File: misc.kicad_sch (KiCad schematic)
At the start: 93 parts, among them CN2 Expansion, CN3 Cartridge, CN5 1P, CN504 AV Out, CN6 1P, IC401 74ACT241, IC701 PIC16F630/18324, IC901 TL974, J1 Barrel_Jack, J2 EXT, Q1 MMBT3904, U1 TPS564257DRLR

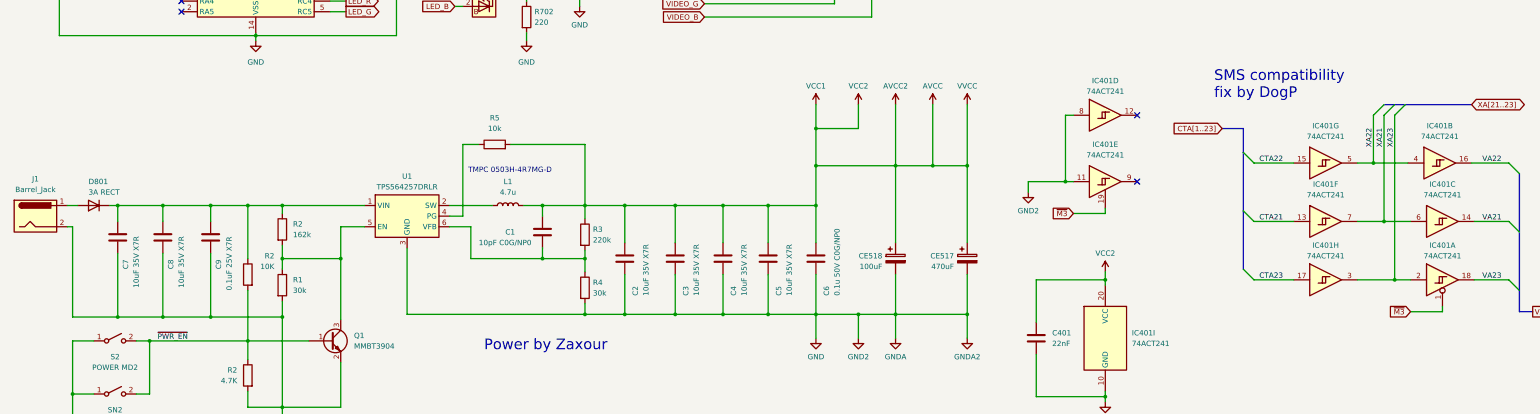
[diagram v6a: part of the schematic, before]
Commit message: More tweaks, documentation. Add hex file for switchless mod.
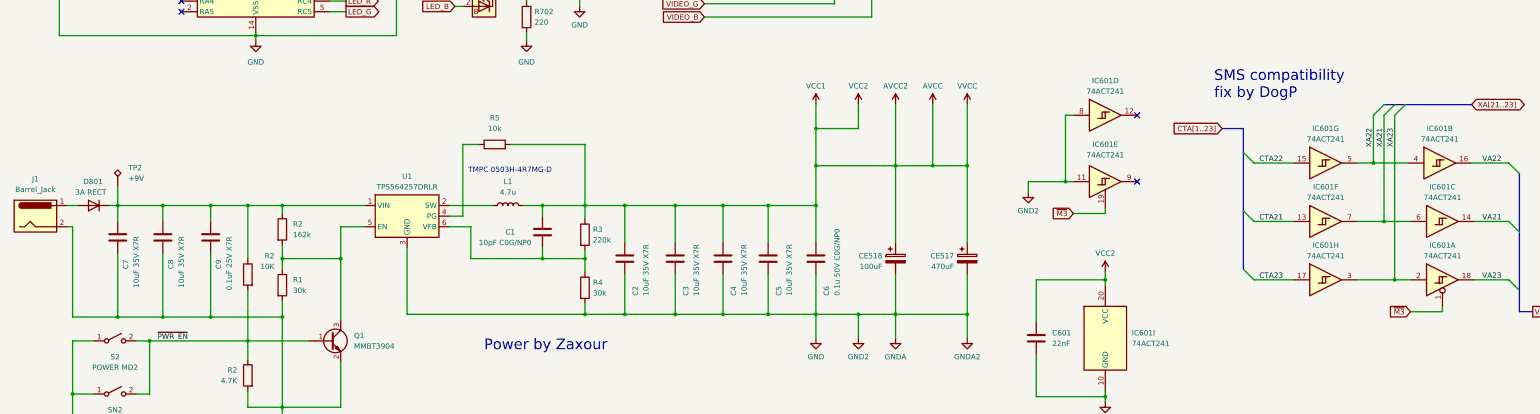
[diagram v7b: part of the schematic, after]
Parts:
- added TP2: +9V, Connector_PinHeader_2.54mm:PinHeader_1x01_P2.54mm_Vertical, symbol Connector:TestPoint_Alt
- renumbered C401 to C601, IC401 to IC601
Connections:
- net at C7.1, C8.1, C9.1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: now also TP2.1
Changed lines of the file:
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@@
     (stroke (width 0) (type default))
   )
+  (wire (pts (xy 44.45 215.9) (xy 44.45 220.345))
+    (stroke (width 0) (type default))
+  )
   (wire (pts (xy 302.26 111.76) (xy 299.72 111.76))
     (stroke (width 0) (type default))
@@
   (symbol (lib_id "74xx:74LS241_Split") (at 361.315 238.125 0) (unit 1)
     (in_bom yes) (on_board yes) (dnp no) (fields_autoplaced)
-    (property "Reference" "IC401" (at 361.315 229.87 0)
+    (property "Reference" "IC601" (at 361.315 229.87 0)
       (effects (font (size 1.27 1.27)))
     )
@@
       (project "Neptune"
         (path "/bcc23b51-b742-4ae5-9dd6-d96a24058944/01513199-62c5-4123-a151-ccd381a5e6c1"
-          (reference "IC401") (unit 1)
+          (reference "IC601") (unit 1)
         )
       )
@@
   (symbol (lib_id "74xx:74LS241_Split") (at 333.375 238.125 0) (unit 8)
     (in_bom yes) (on_board yes) (dnp no) (fields_autoplaced)
-    (property "Reference" "IC401" (at 333.375 229.87 0)
+    (property "Reference" "IC601" (at 333.375 229.87 0)
       (effects (font (size 1.27 1.27)))
     )
@@
       (project "Neptune"
         (path "/bcc23b51-b742-4ae5-9dd6-d96a24058944/01513199-62c5-4123-a151-ccd381a5e6c1"
-          (reference "IC401") (unit 8)
+          (reference "IC601") (unit 8)
         )
       )
@@
   (symbol (lib_id "Device:D") (at 38.735 220.345 180) (unit 1)
     (in_bom yes) (on_board yes) (dnp no)
-    (property "Reference" "D801" (at 37.465 214.63 0)
+    (property "Reference" "D801" (at 36.195 214.63 0)
       (effects (font (size 1.27 1.27)) (justify right))
     )
-    (property "Value" "3A RECT" (at 37.465 217.17 0)
+    (property "Value" "3A RECT" (at 34.29 217.17 0)
       (effects (font (size 1.27 1.27)) (justify right))
     )
@@
   (symbol (lib_id "74xx:74LS241_Split") (at 361.315 224.155 0) (unit 3)
     (in_bom yes) (on_board yes) (dnp no) (fields_autoplaced)
-    (property "Reference" "IC401" (at 361.315 215.265 0)
+    (property "Reference" "IC601" (at 361.315 215.9 0)
       (effects (font (size 1.27 1.27)))
     )
-    (property "Value" "74ACT241" (at 361.315 217.805 0)
+    (property "Value" "74ACT241" (at 361.315 218.44 0)
       (effects (font (size 1.27 1.27)))
     )
@@
       (project "Neptune"
         (path "/bcc23b51-b742-4ae5-9dd6-d96a24058944/01513199-62c5-4123-a151-ccd381a5e6c1"
-          (reference "IC401") (unit 3)
+          (reference "IC601") (unit 3)
         )
       )
@@
   (symbol (lib_id "74xx:74LS241_Split") (at 280.67 214.63 0) (unit 5)
     (in_bom yes) (on_board yes) (dnp no) (fields_autoplaced)
-    (property "Reference" "IC401" (at 280.67 205.74 0)
+    (property "Reference" "IC601" (at 280.67 205.74 0)
       (effects (font (size 1.27 1.27)))
     )
@@
       (project "Neptune"
         (path "/bcc23b51-b742-4ae5-9dd6-d96a24058944/01513199-62c5-4123-a151-ccd381a5e6c1"
-          (reference "IC401") (unit 5)
+          (reference "IC601") (unit 5)
         )
       )
@@
     )
   )
+  (symbol (lib_id "Connector:TestPoint_Alt") (at 44.45 215.9 0) (unit 1)
+    (in_bom yes) (on_board yes) (dnp no) (fields_autoplaced)
+    (property "Reference" "TP2" (at 46.99 211.328 0)
+      (effects (font (size 1.27 1.27)) (justify left))
+    )
+    (property "Value" "+9V" (at 46.99 213.868 0)
+      (effects (font (size 1.27 1.27)) (justify left))
+    )
+    (property "Footprint" "Connector_PinHeader_2.54mm:PinHeader_1x01_P2.54mm_Vertical" (at 49.53 215.9 0)
+      (effects (font (size 1.27 1.27)) hide)
+    )
+    (property "Datasheet" "~" (at 49.53 215.9 0)
+      (effects (font (size 1.27 1.27)) hide)
+    )
+    (pin "1")
+    (instances
+      (project "Neptune"
+        (path "/bcc23b51-b742-4ae5-9dd6-d96a24058944/01513199-62c5-4123-a151-ccd381a5e6c1"
+          (reference "TP2") (unit 1)
+        )
+      )
+    )
+  )
   (symbol (lib_id "Connector_Generic:Conn_01x09") (at 240.03 38.1 0) (mirror y) (unit 1)
     (in_bom yes) (on_board yes) (dnp no) (fields_autoplaced)
@@
   (symbol (lib_id "74xx:74LS241_Split") (at 333.375 210.185 0) (unit 7)
     (in_bom yes) (on_board yes) (dnp no) (fields_autoplaced)
-    (property "Reference" "IC401" (at 333.375 201.295 0)
+    (property "Reference" "IC601" (at 333.375 201.93 0)
       (effects (font (size 1.27 1.27)))
     )
-    (property "Value" "74ACT241" (at 333.375 203.835 0)
+    (property "Value" "74ACT241" (at 333.375 204.47 0)
       (effects (font (size 1.27 1.27)))
     )
@@
       (project "Neptune"
         (path "/bcc23b51-b742-4ae5-9dd6-d96a24058944/01513199-62c5-4123-a151-ccd381a5e6c1"
-          (reference "IC401") (unit 7)
+          (reference "IC601") (unit 7)
         )
       )
@@
   (symbol (lib_id "74xx:74LS241_Split") (at 333.375 224.155 0) (unit 6)
     (in_bom yes) (on_board yes) (dnp no) (fields_autoplaced)
-    (property "Reference" "IC401" (at 333.375 215.265 0)
+    (property "Reference" "IC601" (at 333.375 215.9 0)
       (effects (font (size 1.27 1.27)))
     )
-    (property "Value" "74ACT241" (at 333.375 217.805 0)
+    (property "Value" "74ACT241" (at 333.375 218.44 0)
       (effects (font (size 1.27 1.27)))
     )
@@
       (project "Neptune"
         (path "/bcc23b51-b742-4ae5-9dd6-d96a24058944/01513199-62c5-4123-a151-ccd381a5e6c1"
-          (reference "IC401") (unit 6)
+          (reference "IC601") (unit 6)
         )
       )
@@
   (symbol (lib_id "74xx:74LS241_Split") (at 280.67 198.755 0) (unit 4)
     (in_bom yes) (on_board yes) (dnp no) (fields_autoplaced)
-    (property "Reference" "IC401" (at 280.67 190.5 0)
+    (property "Reference" "IC601" (at 280.67 190.5 0)
       (effects (font (size 1.27 1.27)))
     )
@@
       (project "Neptune"
         (path "/bcc23b51-b742-4ae5-9dd6-d96a24058944/01513199-62c5-4123-a151-ccd381a5e6c1"
-          (reference "IC401") (unit 4)
+          (reference "IC601") (unit 4)
         )
       )
@@
   (symbol (lib_id "74xx:74LS241_Split") (at 360.68 210.185 0) (unit 2)
     (in_bom yes) (on_board yes) (dnp no) (fields_autoplaced)
-    (property "Reference" "IC401" (at 360.68 201.295 0)
+    (property "Reference" "IC601" (at 360.68 201.93 0)
       (effects (font (size 1.27 1.27)))
     )
-    (property "Value" "74ACT241" (at 360.68 203.835 0)
+    (property "Value" "74ACT241" (at 360.68 204.47 0)
       (effects (font (size 1.27 1.27)))
     )
@@
       (project "Neptune"
         (path "/bcc23b51-b742-4ae5-9dd6-d96a24058944/01513199-62c5-4123-a151-ccd381a5e6c1"
-          (reference "IC401") (unit 2)
+          (reference "IC601") (unit 2)
         )
       )
@@
   (symbol (lib_id "74xx:74LS241_Split") (at 280.67 252.095 0) (unit 9)
     (in_bom yes) (on_board yes) (dnp no) (fields_autoplaced)
-    (property "Reference" "IC401" (at 287.02 250.825 0)
+    (property "Reference" "IC601" (at 287.02 250.825 0)
       (effects (font (size 1.27 1.27)) (justify left))
     )
@@
       (project "Neptune"
         (path "/bcc23b51-b742-4ae5-9dd6-d96a24058944/01513199-62c5-4123-a151-ccd381a5e6c1"
-          (reference "IC401") (unit 9)
+          (reference "IC601") (unit 9)
         )
       )
@@
   (symbol (lib_id "Device:C") (at 264.16 252.095 0) (unit 1)
     (in_bom yes) (on_board yes) (dnp no) (fields_autoplaced)
-    (property "Reference" "C401" (at 267.97 250.825 0)
+    (property "Reference" "C601" (at 267.97 250.825 0)
       (effects (font (size 1.27 1.27)) (justify left))
     )
@@
       (project "Neptune"
         (path "/bcc23b51-b742-4ae5-9dd6-d96a24058944/01513199-62c5-4123-a151-ccd381a5e6c1"
-          (reference "C401") (unit 1)
+          (reference "C601") (unit 1)
         )
       )

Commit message: General tweaks, add some DigiKey part numbers.
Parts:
- C1: DigiKey (none) -> 311-4160-1-ND
- C2, C3, C4, C5, C7, C8: DigiKey (none) -> 1276-3103-1-ND
- C9: DigiKey (none) -> 1276-1099-1-ND
- CE27, CE28, CE508, CE509: DigiKey (none) -> 493-13447-1-ND
- IC601: DigiKey (none) -> 296-4384-1-ND
- IC901: DigiKey (none) -> 296-21693-1-ND
- L1: DigiKey (none) -> 490-9760-1-ND
- LED701: renamed from LED1; value LED_GBKR -> GBKR
- Q1: DigiKey (none) -> MMBT3904TPMSCT-ND
- R1, R4: DigiKey (none) -> P30.0KCCT-ND
- R2: DigiKey (none) -> P162KCCT-ND
- R3: DigiKey (none) -> P220KCCT-ND
- R48: DigiKey (none) -> P2.20KCCT-ND
- R602: DigiKey (none) -> P3.30KCCT-ND
- R702: DigiKey (none) -> P220CCT-ND
- U1: DigiKey (none) -> 296-TPS564257DRLRCT-ND
